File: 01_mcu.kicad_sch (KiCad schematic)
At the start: 3 parts, among them J2 UART, J3 SWD, U3 Pico

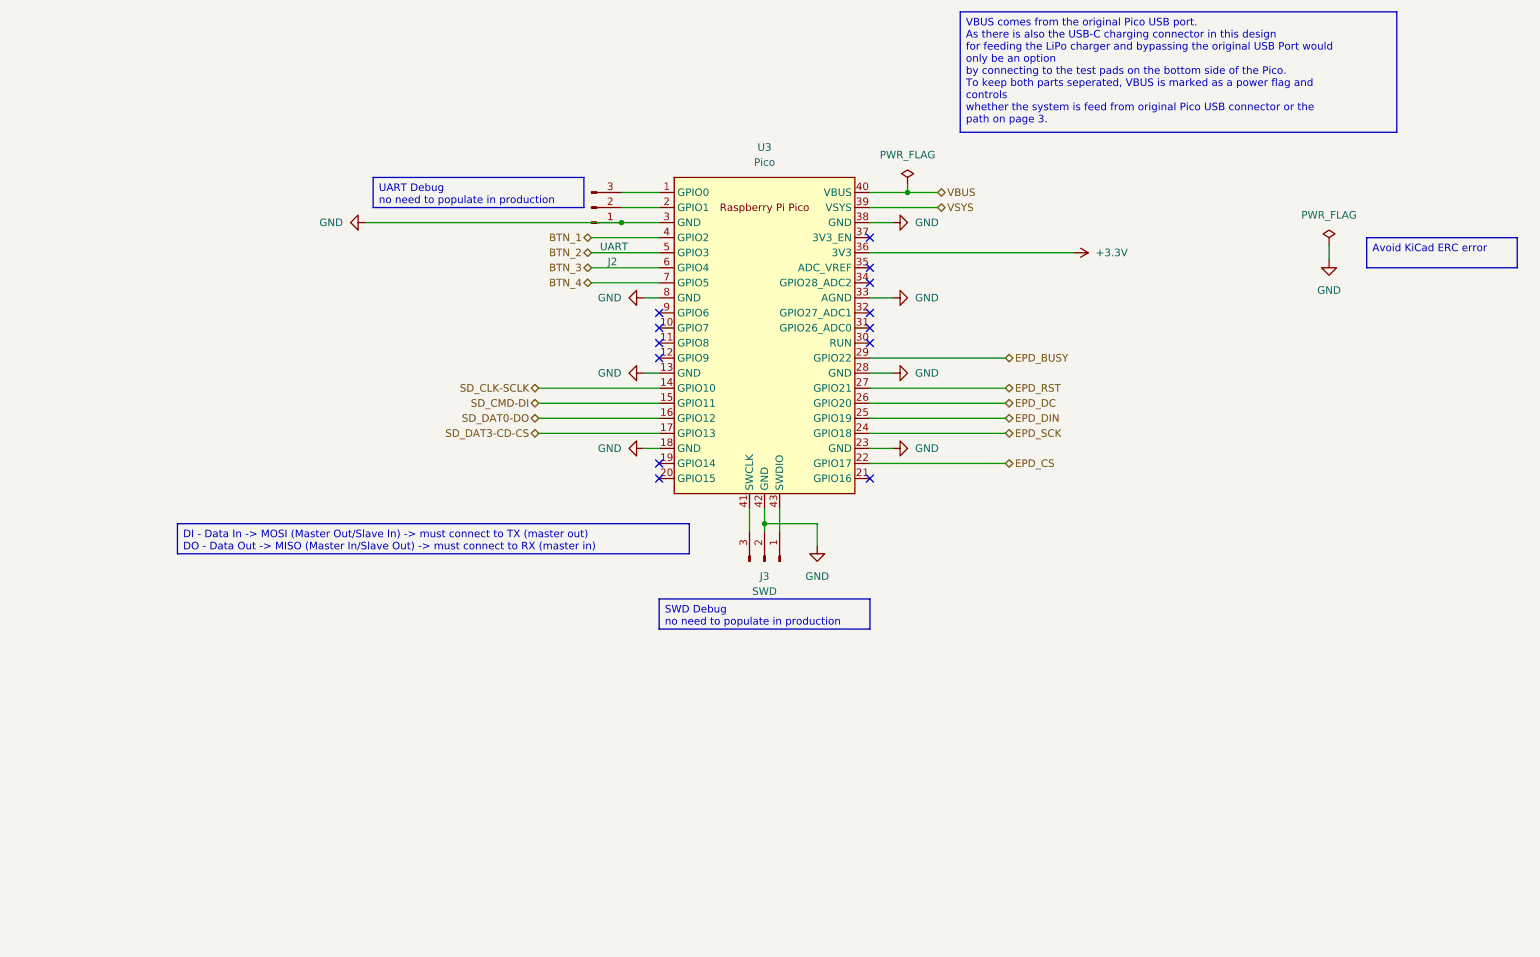
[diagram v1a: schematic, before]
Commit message: switch to KiCad Pico extended symbol
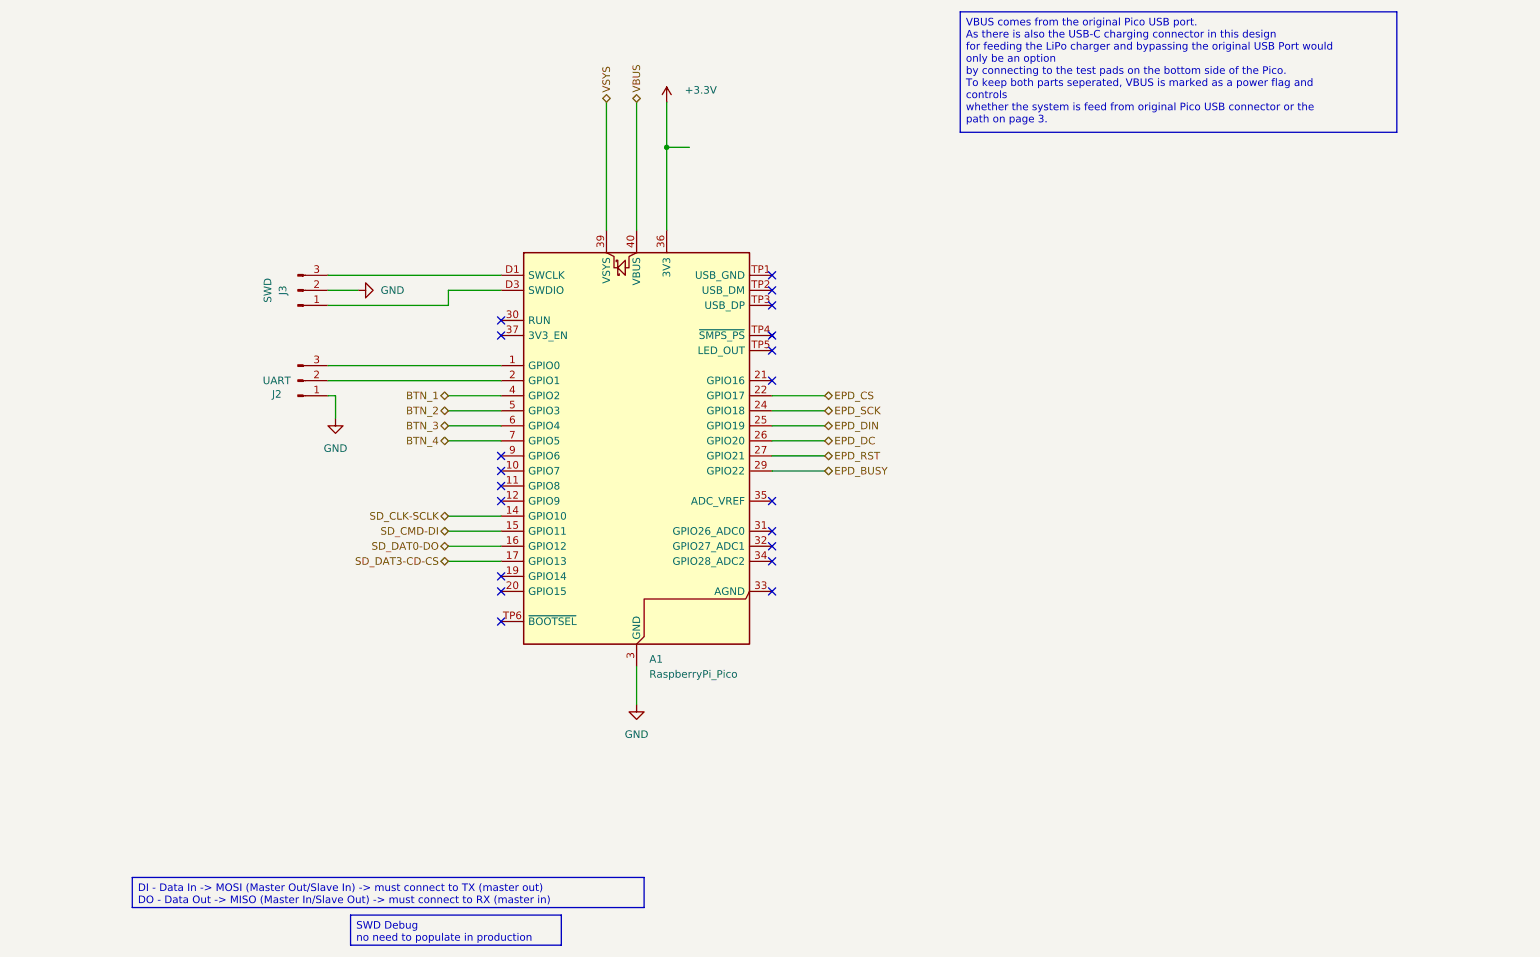
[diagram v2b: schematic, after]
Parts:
- removed U3: Pico, prj-footprints:RPi_Pico_SMD_TH, symbol MCU_RaspberryPi_and_Boards:Pico
- added A1: RaspberryPi_Pico, Module:RaspberryPi_Pico_SMD, symbol MCU_Module:RaspberryPi_Pico_Extensive
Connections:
- net +3.3V: now also A1.36 (3V3)
- net BTN_1: now also A1.4 (GPIO2)
- net BTN_2: now also A1.5 (GPIO3)
- net BTN_3: now also A1.6 (GPIO4)
- net BTN_4: now also A1.7 (GPIO5)
- net EPD_BUSY: now also A1.29 (GPIO22)
- net EPD_CS: now also A1.22 (GPIO17)
- net EPD_DC: now also A1.26 (GPIO20)
- net EPD_DIN: now also A1.25 (GPIO19)
- net EPD_RST: now also A1.27 (GPIO21)
- net EPD_SCK: now also A1.24 (GPIO18)
- net GND: now also A1.13 (GND), A1.18 (GND), A1.23 (GND), A1.28 (GND), A1.3 (GND), A1.38 (GND), A1.8 (GND), A1.D2 (GND)
- net SD_CLK-SCLK: now also A1.14 (GPIO10)
- net SD_CMD-DI: now also A1.15 (GPIO11)
- net SD_DAT0-DO: now also A1.16 (GPIO12)
- net SD_DAT3-CD-CS: now also A1.17 (GPIO13)
- net VBUS: now also A1.40 (VBUS)
- net VSYS: now also A1.39 (VSYS)
- net at J2.3 (Pin_3): now also A1.1 (GPIO0)
- net at J2.2 (Pin_2): now also A1.2 (GPIO1)
- net at J3.3 (Pin_3): now also A1.D1 (SWCLK)
- net at J3.1 (Pin_1): now also A1.D3 (SWDIO)
- no-connect marks 13 -> 20
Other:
- moved on the sheet: J2, J3

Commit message: fully connect the sd connector, redraw sd and buttons
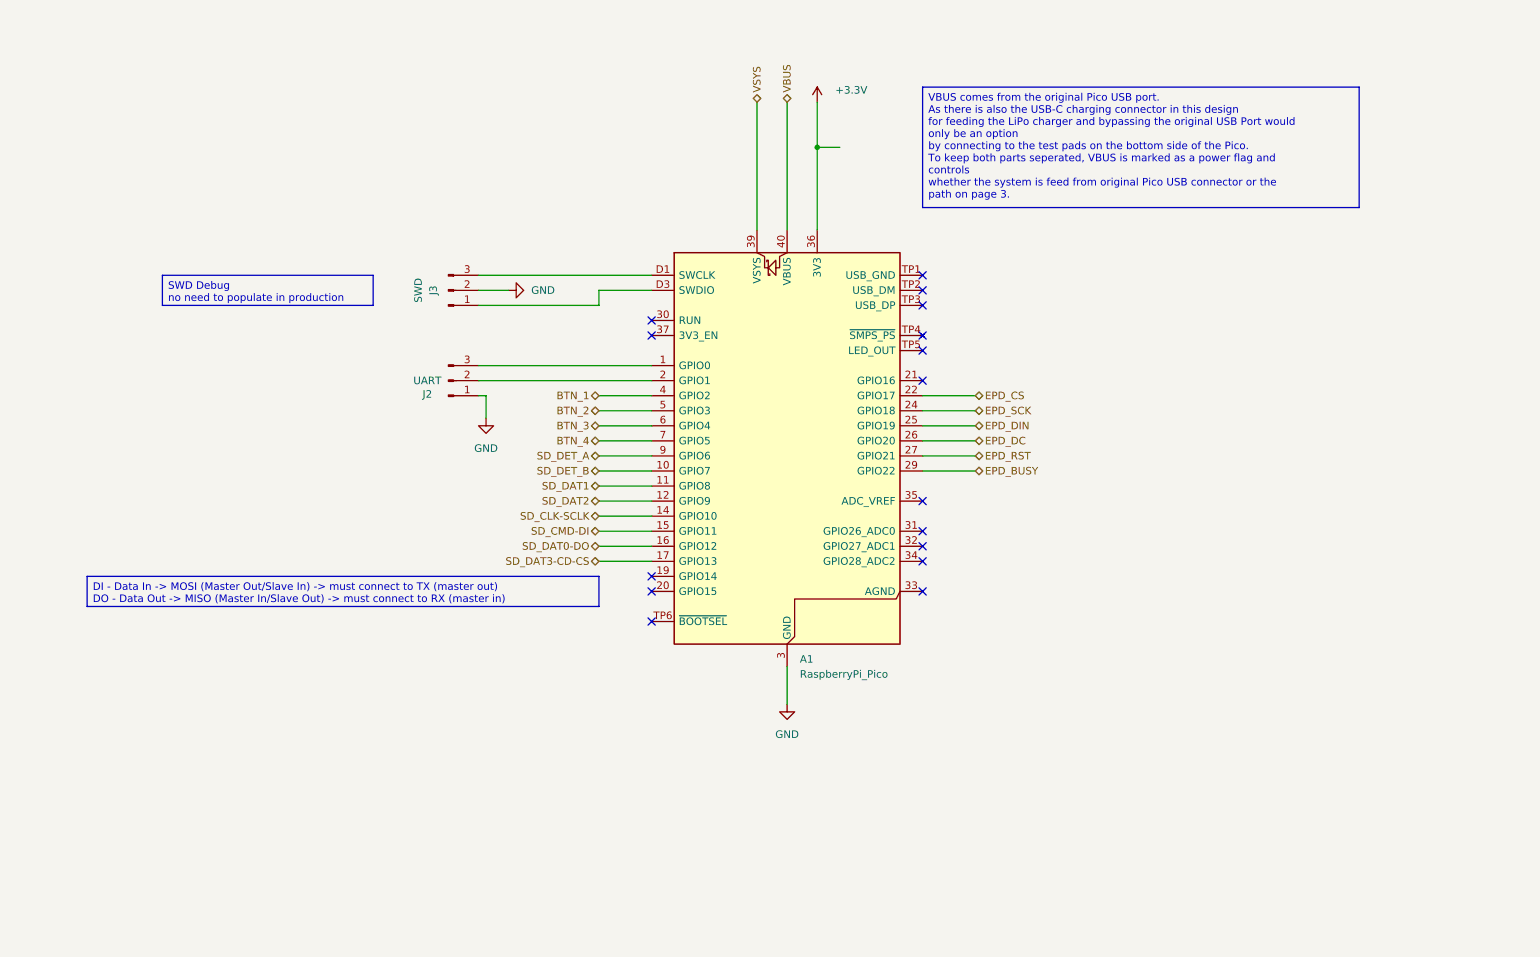
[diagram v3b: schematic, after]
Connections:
- net SD_DET_B: now reaches A1.10 (GPIO7)
- net SD_DAT1: now reaches A1.11 (GPIO8)
- net SD_DAT2: now reaches A1.12 (GPIO9)
- net SD_DET_A: now reaches A1.9 (GPIO6)
- no-connect marks 20 -> 16
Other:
- moved on the sheet: A1, J2, J3

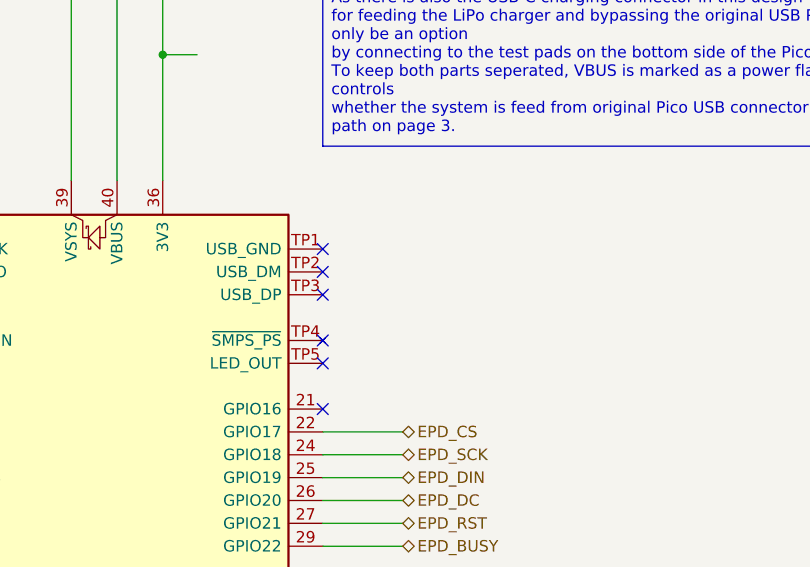
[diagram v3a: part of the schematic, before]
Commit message: updated power path, connect USB-C to pico's USB data
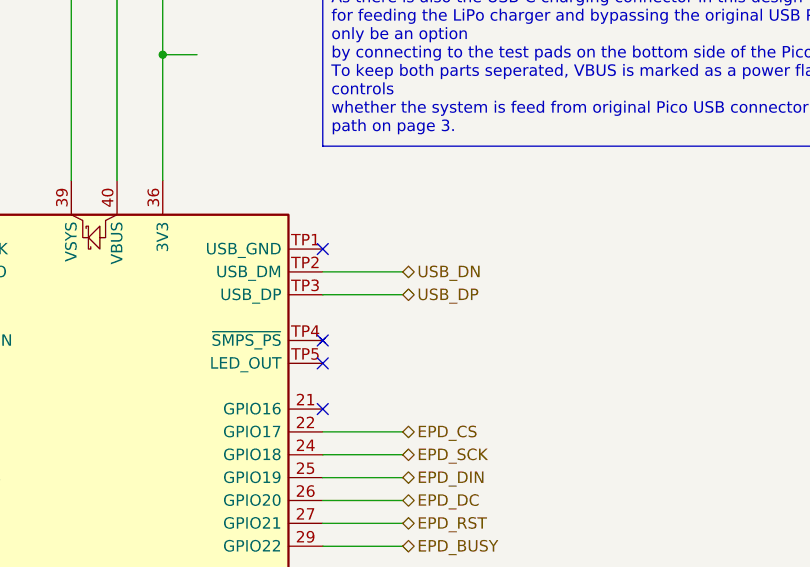
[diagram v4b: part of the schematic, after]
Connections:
- net USB_DN: now reaches A1.TP2 (USB_DM)
- net USB_DP: now reaches A1.TP3 (USB_DP)
- no-connect marks 16 -> 14
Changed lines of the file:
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@@
-	)
-	(no_connect
-		(at 168.91 72.39)
 	)
 	(no_connect
@@
 	)
 	(no_connect
-		(at 168.91 69.85)
-	)
-	(no_connect
 		(at 123.19 125.73)
 	)
@@
 	)
 	(no_connect
+		(at 168.91 67.31)
+	)
+	(no_connect
 		(at 168.91 80.01)
 	)
@@
 	)
 	(no_connect
-		(at 168.91 67.31)
-	)
-	(no_connect
 		(at 168.91 113.03)
 	)
@@
 	(wire
 		(pts
+			(xy 168.91 69.85) (xy 177.8 69.85)
+		)
+		(stroke
+			(width 0)
+			(type default)
+		)
+	)
+	(wire
+		(pts
 			(xy 93.98 82.55) (xy 123.19 82.55)
 		)
@@
 	(wire
 		(pts
+			(xy 168.91 72.39) (xy 177.8 72.39)
+		)
+		(stroke
+			(width 0)
+			(type default)
+		)
+	)
+	(wire
+		(pts
 			(xy 99.06 69.85) (xy 93.98 69.85)
 		)
@@
 		)
 	)
+	(hierarchical_label "USB_DP"
+		(shape bidirectional)
+		(at 177.8 72.39 0)
+		(effects
+			(font
+				(size 1.27 1.27)
+			)
+			(justify left)
+		)
+	)
 	(hierarchical_label "SD_DAT2"
 		(shape bidirectional)
@@
 		(effects
 			(font
+				(size 1.27 1.27)
+			)
+			(justify left)
+		)
+	)
+	(hierarchical_label "USB_DN"
+		(shape bidirectional)
+		(at 177.8 69.85 0)
+		(effects
+			(font

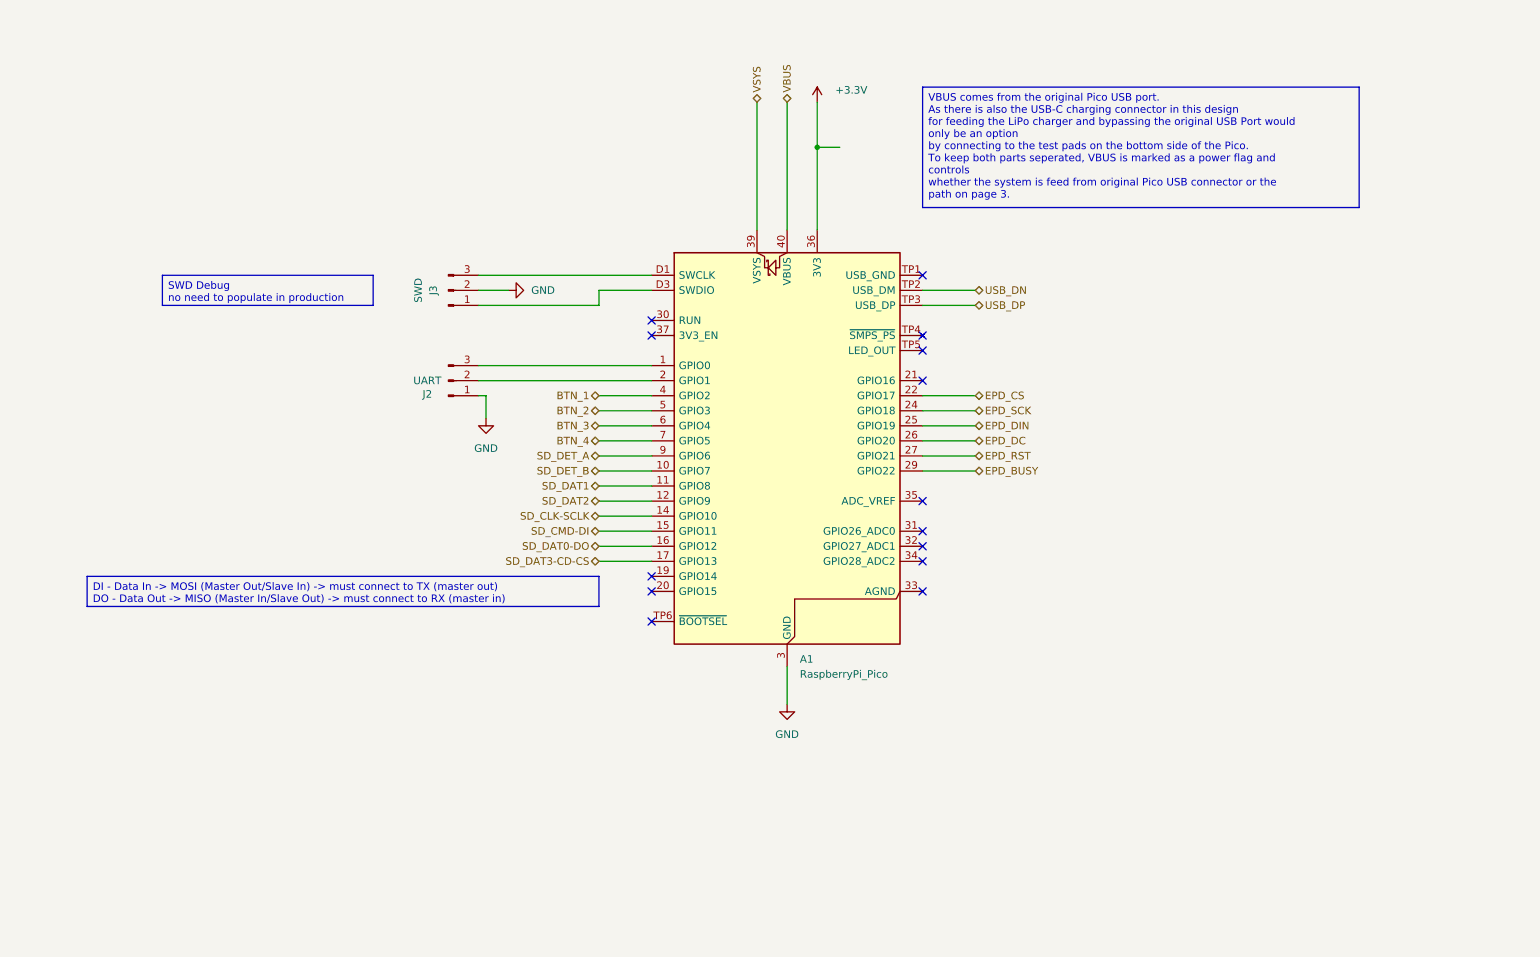
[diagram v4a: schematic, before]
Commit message: v2: major changes
- Move to hierarchical labels
- use another RP Pico Footprint
- split power path in USB/charging and on/off with a button approach in order to control turning on and off
  with the RP Pico, make use of long presses and delay turning of the voltage in order to do a proper shutdown
- introduce another charging controller with a better performance an a lower voltage needed in order to charge the battery
- rework display booster circuit
- rework SD and buttons
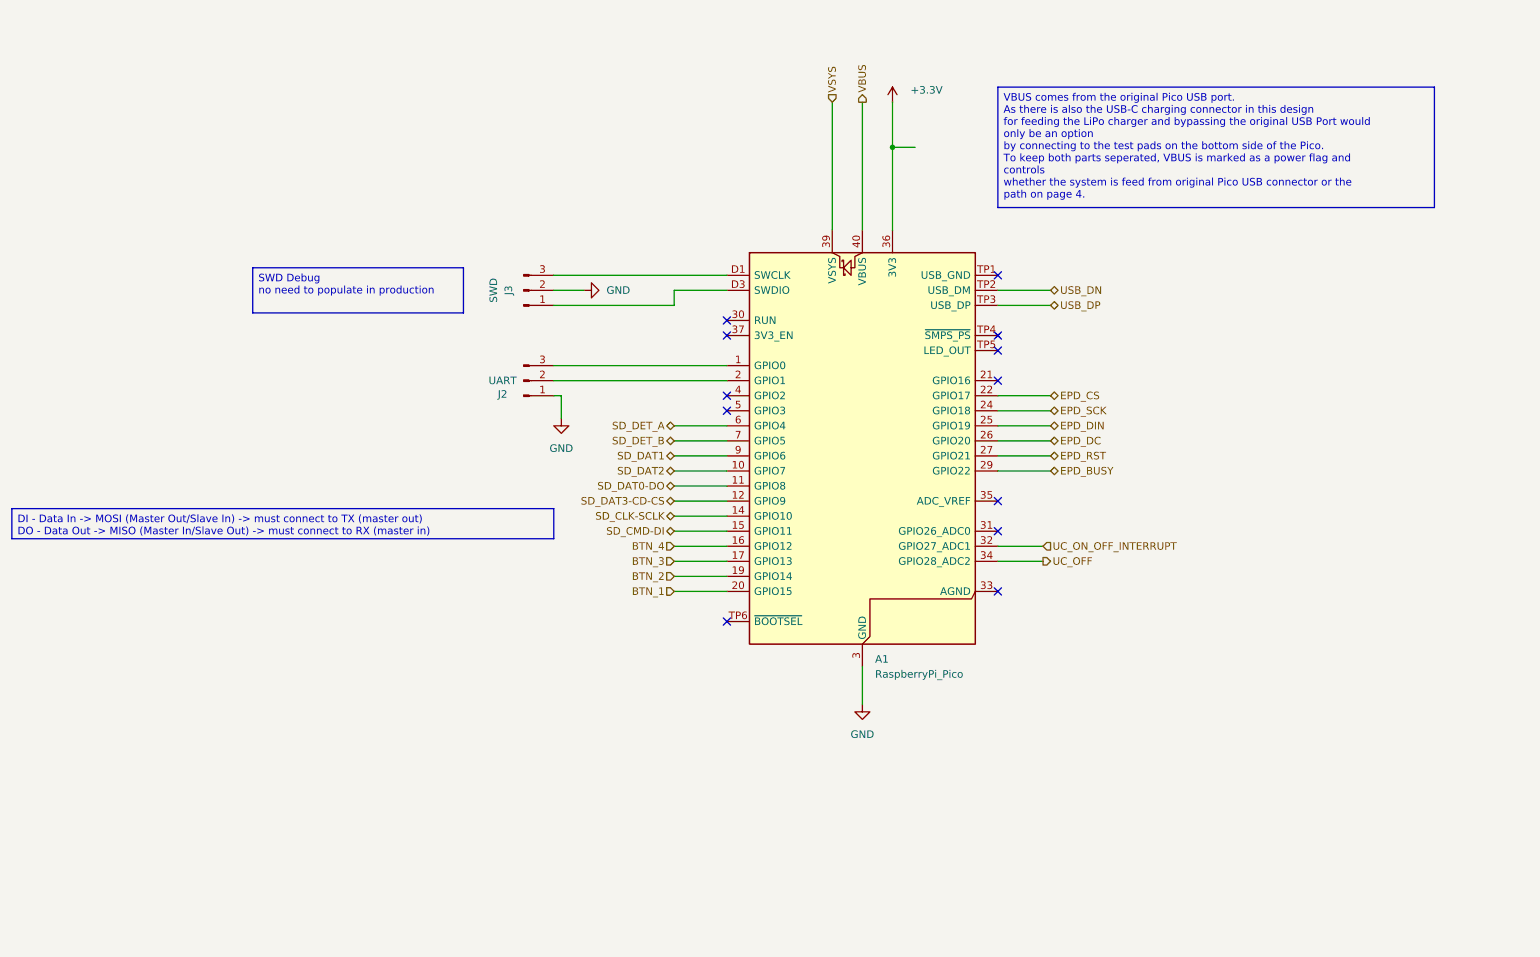
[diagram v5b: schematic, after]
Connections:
- net BTN_1: now also A1.20 (GPIO15); no longer A1.4 (GPIO2)
- net BTN_2: now also A1.19 (GPIO14); no longer A1.5 (GPIO3)
- net BTN_3: now also A1.17 (GPIO13); no longer A1.6 (GPIO4)
- net BTN_4: now also A1.16 (GPIO12); no longer A1.7 (GPIO5)
- net SD_DAT0-DO: now also A1.11 (GPIO8); no longer A1.16 (GPIO12)
- net SD_DAT1: now also A1.9 (GPIO6); no longer A1.11 (GPIO8)
- net SD_DAT2: now also A1.10 (GPIO7); no longer A1.12 (GPIO9)
- net SD_DAT3-CD-CS: now also A1.12 (GPIO9); no longer A1.17 (GPIO13)
- net SD_DET_A: now also A1.6 (GPIO4); no longer A1.9 (GPIO6)
- net SD_DET_B: now also A1.7 (GPIO5); no longer A1.10 (GPIO7)
- net UC_ON_OFF_INTERRUPT: now reaches A1.32 (GPIO27_ADC1)
- net UC_OFF: now reaches A1.34 (GPIO28_ADC2)
- no-connect marks 14 -> 12
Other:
- moved on the sheet: A1, J2, J3
